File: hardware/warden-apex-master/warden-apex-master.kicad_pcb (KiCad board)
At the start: 4 copper layers, 100 x 100 mm, 72 parts, among them IC1 SIM7080G, IC2 BQ24650RVAR, IC3 TPS63070RNMR, IC4 MAX98357AETE+T, J1 U.FL-R-SMT-1, J2 U.FL-R-SMT-1, J3 61300211121, Q1 DMG9926UDM, Q2 AO3401A, Q3 2N7002, U1 113991115, U2 Ai-Thinker-Ra-01, U3 M138 Modem, U4 MCP23017_SO, U5 SRV05-4-P-T7, U6 SC16IS740, X1 14.7456MHz

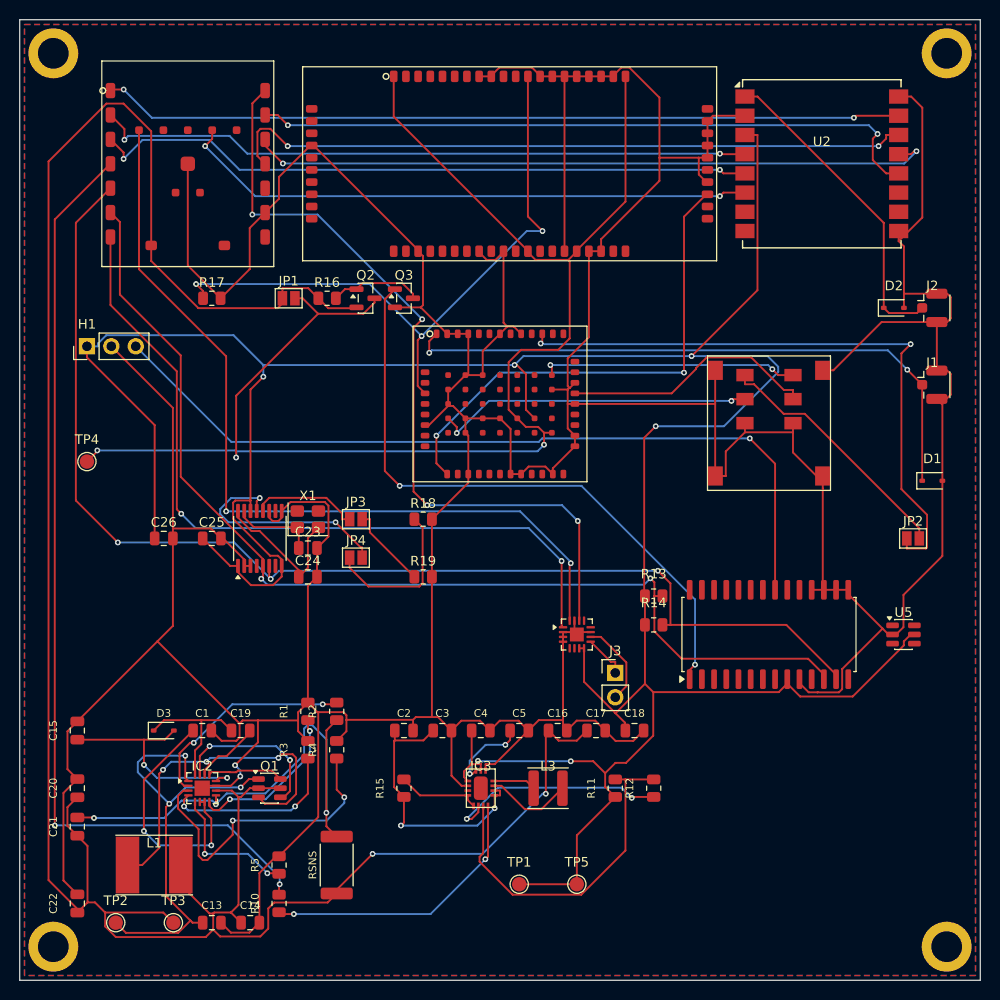
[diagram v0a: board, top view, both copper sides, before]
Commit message: Update warden-apex design with new components and net classifications. Added multiple capacitors (C27, C28, C29, C30, C31, C32) and a resistor (R23) to the schematic and PCB. Updated net classes for improved clarity and organization. Adjusted timestamps and documentation in PLAN.md and VARIANTS.md to reflect the latest changes.
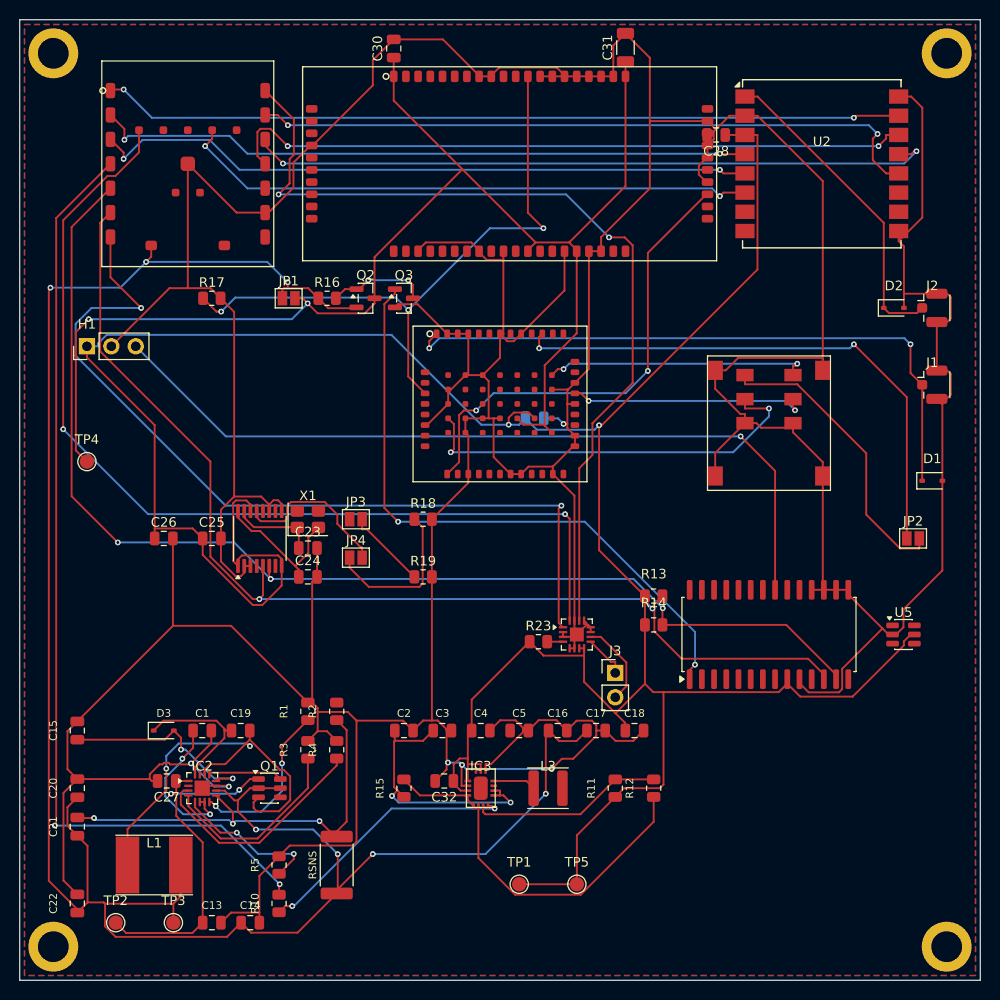
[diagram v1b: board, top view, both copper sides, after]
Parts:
- added C27: 100nF, Capacitor_SMD:C_0805_2012Metric, F.Cu at (15.3, 79.2)
- added C28: 100nF, Capacitor_SMD:C_0805_2012Metric, F.Cu at (72.5, 12.0)
- added C29: 100nF, Capacitor_SMD:C_0805_2012Metric, B.Cu at (53.6, 41.5)
- added C30: 100nF, Capacitor_SMD:C_0805_2012Metric, F.Cu at (38.9, 3.00)
- added C31: 47uF, C_1206_3216Metric, F.Cu at (63.1, 2.90)
- added C32: 10uF, Capacitor_SMD:C_0805_2012Metric, F.Cu at (44.2, 79.2)
- added R23: 100k, Resistor_SMD:R_0805_2012Metric, F.Cu at (54.0, 64.8)
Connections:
- IC4 pad 12: (no net) -> /GND
- IC4 pad 13: (no net) -> /GND
- IC4 pad 4: /GND -> /SD_MODE
- IC4 pad 5: (no net) -> /GND
- IC4 pad 6: (no net) -> /GND
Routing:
- net /GND: track 667.2 -> 736.5 mm, vias 2 -> 6
- net /VBAT_SYS: track 255.8 -> 226.4 mm, vias 2 -> 7
- net /MPPSET: track 22.6 -> 0.00 mm, vias 2 -> 0
- net /CHG_GATE_HI: track 16.8 -> 0.00 mm, vias 2 -> 0
- net /FB_DIV: track 35.9 -> 20.0 mm
- net /I2S_BCLK: track 87.7 -> 102.1 mm
- net /MODEM_VBAT_SW: track 155.0 -> 142.8 mm, vias 3 -> 2
- net /3V3: track 313.4 -> 302.0 mm, vias 6 -> 2
- net /U6_UART_TX: track 11.3 -> 0.00 mm
- net /I2S_LRCLK: track 82.8 -> 93.1 mm, vias 4 -> 2
- net /SOLAR_IN: track 47.5 -> 37.4 mm, vias 3 -> 2
- net /CHG_REF: track 25.5 -> 15.5 mm
- net /CHG_SENSE_NEG: track 54.0 -> 44.5 mm
- net /SIM_RST: track 33.4 -> 42.9 mm
- net /I2S_DOUT: track 80.5 -> 89.5 mm
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
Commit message: Update warden-apex design with new components including F1 (500mA PTC fuse), J4 (Expansion Header), and J5 (Qwiic connector). Adjusted resistor values and footprints for C31 and R24. Updated BOM files and Gerber generation timestamps to reflect the latest changes.
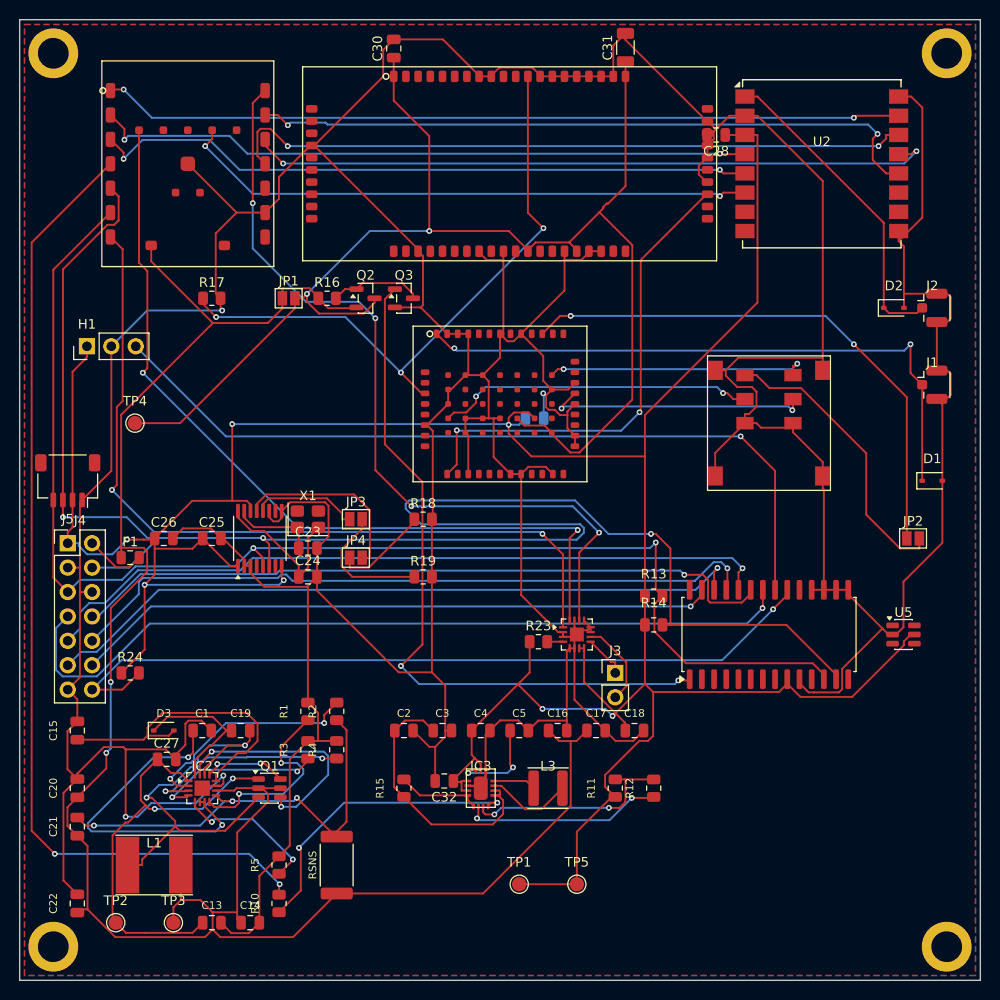
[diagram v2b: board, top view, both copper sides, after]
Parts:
- added F1: 500mA_PTC, Fuse_0805_2012Metric, F.Cu at (11.5, 56.0)
- added J4: Expansion_Header, PinHeader_2x07_P2.54mm_Vertical, F.Cu at (5.00, 54.5)
- added J5: Qwiic, JST_SH_SM04B-SRSS-TB_1x04-1MP_P1.00mm_Horizontal, F.Cu at (5.00, 48.0)
- added R24: 10k, R_0805_2012Metric, F.Cu at (11.5, 68.0)
- moved TP4 6.40 mm to (12.0, 42.0)
- moved C27 2.25 mm to (15.3, 77.0), turned to 0 degrees
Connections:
- IC2 pad : (no net) -> /GND
- IC3 pad 16: (no net) -> /GND
- IC4 pad : (no net) -> /GND
- U4 pad 20: (no net) -> /EXP_IRQ
- U4 pad 22: (no net) -> /EXP_GP1
- U4 pad 23: (no net) -> /EXP_GP2
- U4 pad 24: (no net) -> /EXP_GP3
- U4 pad 25: (no net) -> /EXP_GP4
- U4 pad 26: (no net) -> /EXP_GP5
- U4 pad 27: (no net) -> /EXP_GP6
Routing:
- net /EXP_GP1: track 0.00 -> 84.8 mm, vias 0 -> 1
- net /EXP_IRQ: track 0.00 -> 82.6 mm, vias 0 -> 1
- net /EXP_GP3: track 0.00 -> 77.7 mm, vias 0 -> 1
- net /EXP_GP5: track 0.00 -> 74.3 mm, vias 0 -> 1
- net /EXP_GP2: track 0.00 -> 74.0 mm, vias 0 -> 1
- net /EXP_GP4: track 0.00 -> 73.4 mm, vias 0 -> 1
- net /EXP_GP6: track 0.00 -> 67.1 mm, vias 0 -> 1
- net /I2C_SDA: track 124.0 -> 183.1 mm
- net /CHG_GATE_HI: track 0.00 -> 24.4 mm, vias 0 -> 2
- net /MPPSET: track 0.00 -> 23.6 mm, vias 0 -> 2
- net /3V3: track 302.0 -> 323.5 mm, vias 2 -> 7
- net /I2C_SCL: track 117.1 -> 138.1 mm
- net /CHG_REF: track 15.5 -> 34.8 mm
- net /VBAT_SYS: track 226.4 -> 210.1 mm, vias 7 -> 2
- net /I2S_BCLK: track 102.1 -> 87.7 mm
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
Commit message: Update warden-apex design with new resistor values and components. Changed C5 to 1uF and added resistors R20 (7.15k) and R21 (10k) to the schematic. Updated BOM files to reflect these changes and adjusted Gerber generation timestamps for consistency.
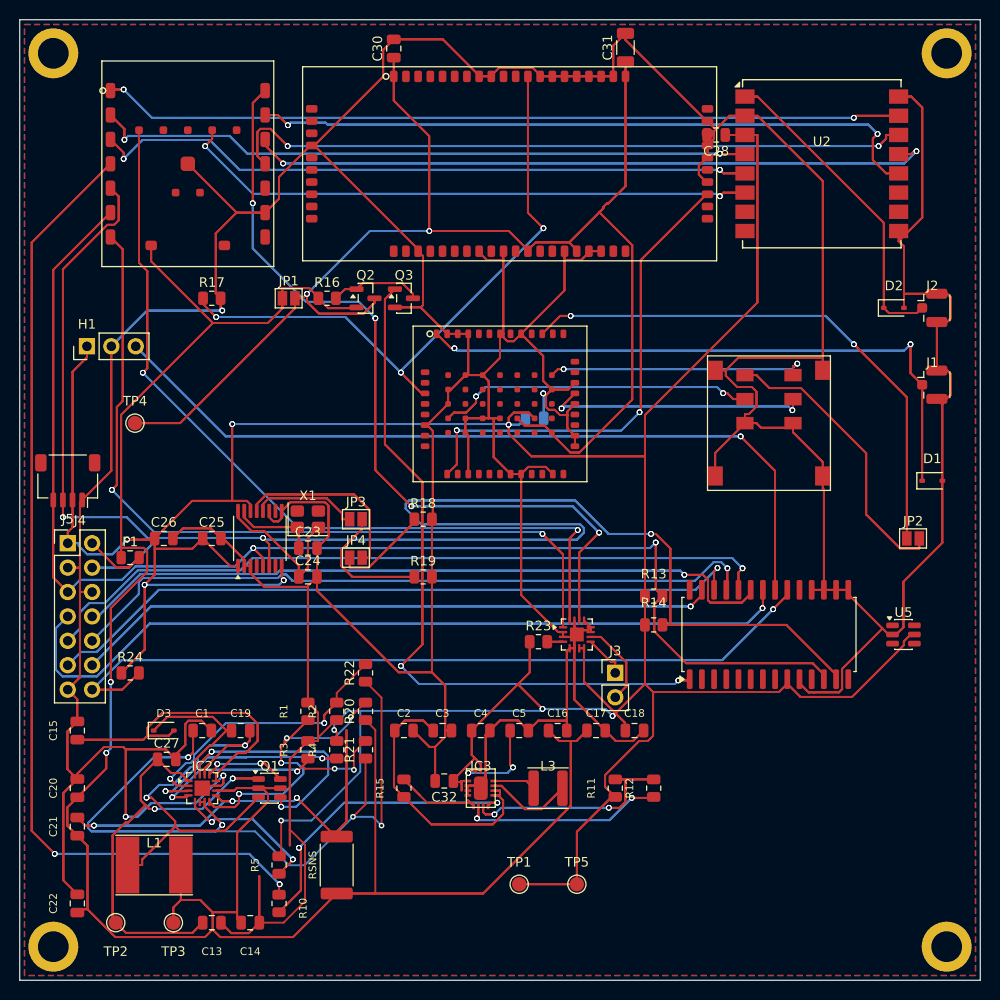
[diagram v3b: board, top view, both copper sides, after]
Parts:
- added R20: 7.15k, Resistor_SMD:R_0805_2012Metric, F.Cu at (36.0, 72.0)
- added R21: 10k, Resistor_SMD:R_0805_2012Metric, F.Cu at (36.0, 76.0)
- added R22: 100k, Resistor_SMD:R_0805_2012Metric, F.Cu at (36.0, 68.0)
- C5: value 100nF -> 1uF
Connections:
- IC3 pad 3: /3V3 -> /GND
- IC3 pad 4: /REG_EN -> /GND
- R2 pad 1: /CHG_SENSE_NEG -> /GND
- R4 pad 2: /GND -> /3V3
- R5 pad 2: /GND -> /3V3
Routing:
- net /GND: track 733.0 -> 1471.8 mm, vias 4 -> 8
- net /3V3: track 323.5 -> 690.3 mm, vias 7 -> 16
- net /VBAT_SYS: track 210.1 -> 438.7 mm, vias 2 -> 4
- net /I2C_SDA: track 183.1 -> 366.1 mm, vias 3 -> 6
- net /MODEM_VBAT_SW: track 143.5 -> 287.1 mm, vias 2 -> 4
- net /I2C_SCL: track 138.1 -> 276.2 mm, vias 2 -> 4
- net /PG_MON: track 102.1 -> 204.1 mm, vias 2 -> 4
- net /I2S_BCLK: track 87.7 -> 175.3 mm, vias 2 -> 4
- net /EXP_GP1: track 84.8 -> 169.5 mm, vias 1 -> 2
- net /I2S_DOUT: track 84.6 -> 169.3 mm, vias 2 -> 4
- net /I2S_LRCLK: track 84.6 -> 169.1 mm, vias 4 -> 8
- net /PIR_SIG: track 84.3 -> 168.6 mm, vias 1 -> 2
- net /LORA_NSS: track 83.4 -> 166.8 mm, vias 2 -> 4
- net /EXP_IRQ: track 82.6 -> 165.2 mm, vias 1 -> 2
- net /CHG_REF: track 34.8 -> 113.0 mm, vias 2 -> 6
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
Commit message: Update warden-apex design with revised net names and routing adjustments. Renamed net SIM_VDD_HOLDER to SIM_VDD_EXT and updated associated nodes. Adjusted timestamps in Gerber files and documentation for consistency. Added notes for manual routing requirements in README.md.
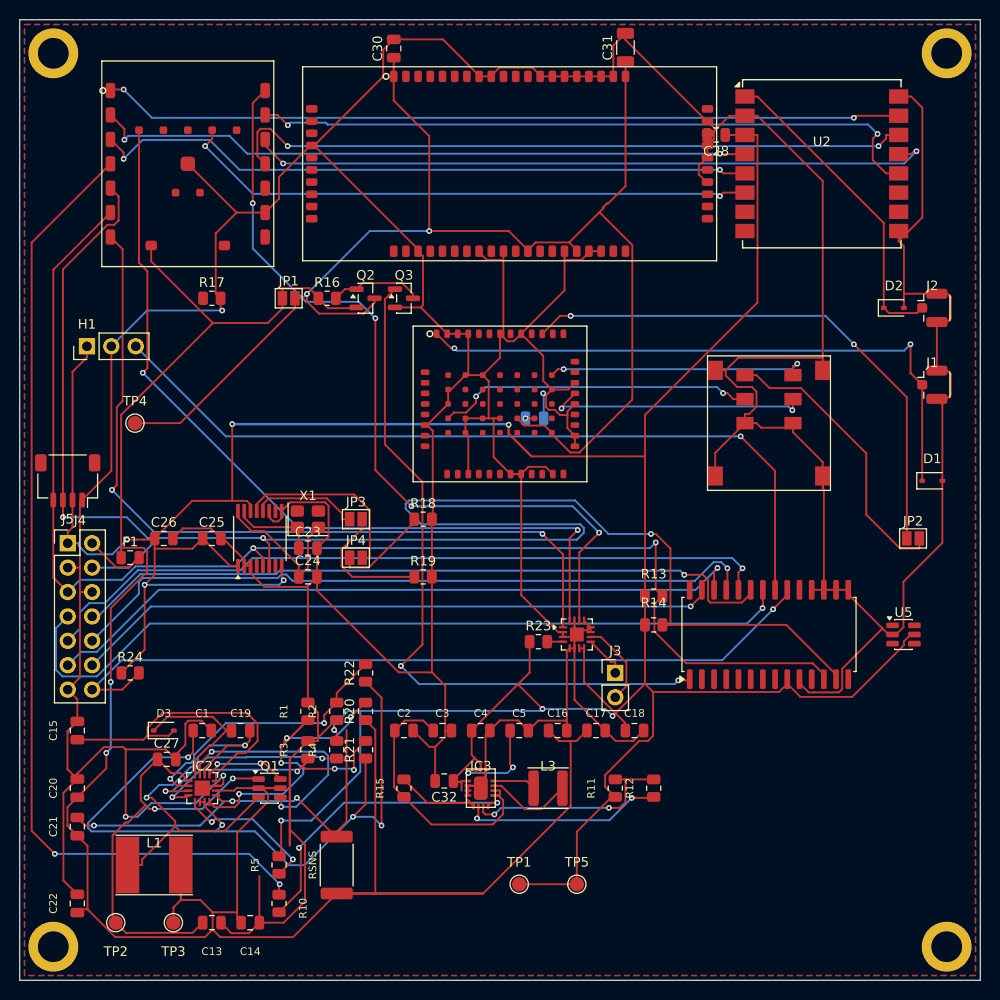
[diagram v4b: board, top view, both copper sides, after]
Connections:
- C29 pad 1: /3V3 -> /SIM_VDD_EXT
- IC1 pad 69: /3V3 -> /SIM_VDD_EXT
- IC2 pad : /GND -> (no net)
- IC4 pad : /GND -> (no net)
- U1 pad 18: (no net) -> /UART1_RX
- U1 pad 19: (no net) -> /UART1_TX
- U3 pad 12: /UART1_RX -> /UART2_RX
- U3 pad 28: /UART1_TX -> /UART2_TX
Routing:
- net /GND: track 1471.8 -> 758.6 mm, vias 8 -> 4
- net /3V3: track 690.3 -> 361.5 mm, vias 16 -> 9
- net /VBAT_SYS: track 438.7 -> 249.4 mm, vias 4 -> 2
- net /I2C_SDA: track 366.1 -> 183.1 mm, vias 6 -> 3
- net /MODEM_VBAT_SW: track 287.1 -> 143.5 mm, vias 4 -> 2
- net /I2C_SCL: track 276.2 -> 138.1 mm, vias 4 -> 2
- net /UART1_RX: track 130.3 -> 0.00 mm, vias 6 -> 0
- net /PG_MON: track 204.1 -> 102.1 mm, vias 4 -> 2
- net /UART1_TX: track 101.0 -> 0.00 mm, vias 4 -> 0
- net /I2S_BCLK: track 175.3 -> 87.7 mm, vias 4 -> 2
- net /EXP_GP1: track 169.5 -> 84.8 mm, vias 2 -> 1
- net /I2S_DOUT: track 169.3 -> 84.6 mm, vias 4 -> 2
- net /I2S_LRCLK: track 169.1 -> 84.6 mm, vias 8 -> 4
- net /PIR_SIG: track 168.6 -> 84.3 mm, vias 2 -> 1
- net /LORA_NSS: track 166.8 -> 83.4 mm, vias 4 -> 2
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- added copper zone on B.Cu, net /GND
- added copper zone on F.Cu, net /GND
- added copper zone on In1.Cu, net /GND
- added copper zone on In2.Cu, net /VBAT_SYS
- removed copper zone on B.Cu, net GND
- removed copper zone on F.Cu, net GND
- removed copper zone on In1.Cu, net GND
- removed copper zone on In2.Cu, net VBAT_SYS

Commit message: Update warden-apex design for Phase 21 SIM7080 repair. Adjusted BOM files to include new capacitor C33 and updated component placements for C34. Revised Gerber files with new timestamps and corrected net connections for UART signals. Enhanced README.md with details on the repair process and updated upload instructions for JLCPCB.
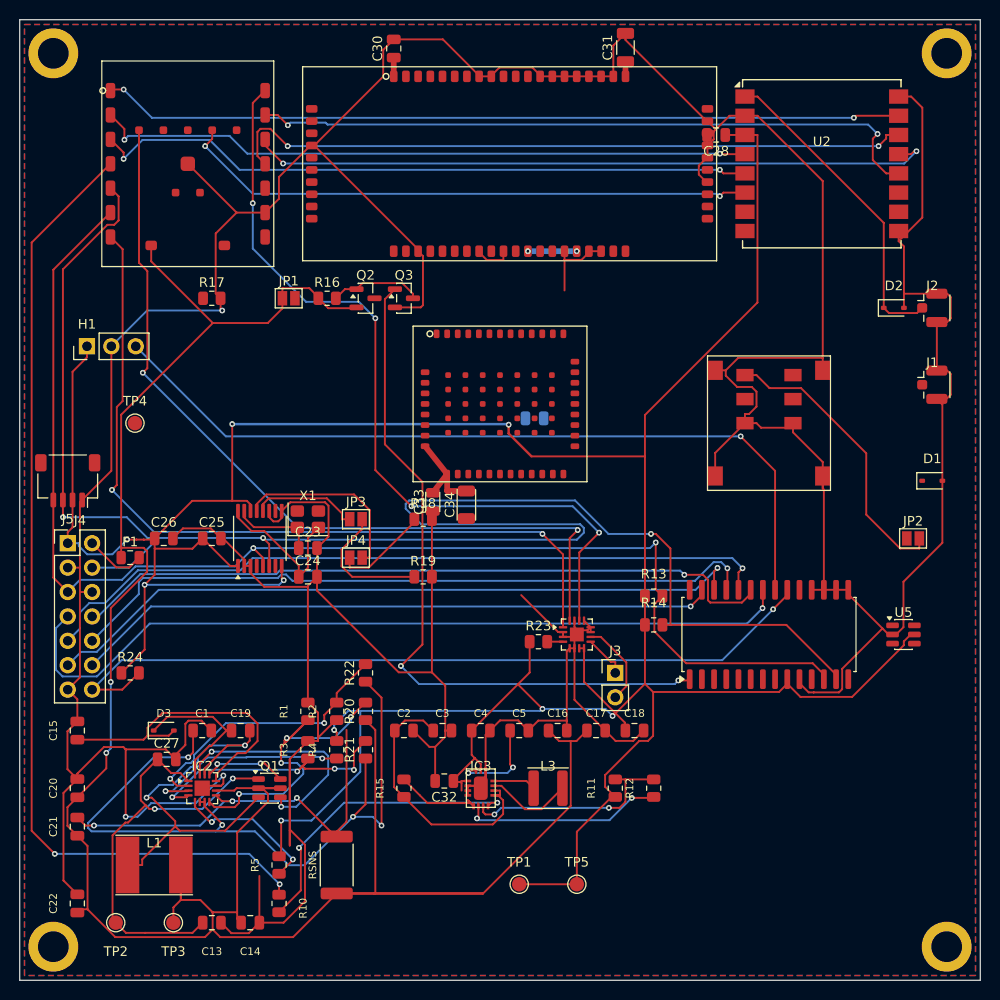
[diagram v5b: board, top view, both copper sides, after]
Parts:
- added C33: 100nF, Capacitor_SMD:C_0805_2012Metric, F.Cu at (43.0, 50.2)
- added C34: 47uF, Capacitor_SMD:C_1206_3216Metric, F.Cu at (46.5, 50.5)
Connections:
- IC1 pad 1: /CELL_RF -> /UART1_RX
- IC1 pad 10: (no net) -> /GND
- IC1 pad 11: /SIM_VDD -> /GND
- IC1 pad 12: (no net) -> /GND
- IC1 pad 13: (no net) -> /GND
- IC1 pad 14: (no net) -> /GND
- IC1 pad 15: (no net) -> /SIM_DATA
- IC1 pad 16: /GND -> /SIM_CLK
- IC1 pad 17: /SIM_DATA -> /SIM_RST
- IC1 pad 18: /GND -> /SIM_VDD
- IC1 pad 19: (no net) -> /GND
- IC1 pad 2: /GND -> /UART1_TX
- IC1 pad 20: (no net) -> /GND
- IC1 pad 23: (no net) -> /GND
- IC1 pad 25: (no net) -> /GND
- IC1 pad 26: (no net) -> /GND
- IC1 pad 29: (no net) -> /GND
- IC1 pad 30: (no net) -> /GND
- IC1 pad 31: (no net) -> /GND
- IC1 pad 32: /GND -> /CELL_RF
- IC1 pad 33: (no net) -> /GND
- IC1 pad 34: /UART1_TX -> /MODEM_VBAT_SW
- IC1 pad 35: (no net) -> /MODEM_VBAT_SW
- IC1 pad 36: (no net) -> /GND
- IC1 pad 38: (no net) -> /GND
- IC1 pad 39: (no net) -> /GND
- IC1 pad 40: /UART1_RX -> /SIM_VDD_EXT
- IC1 pad 41: (no net) -> /GND
- IC1 pad 42: (no net) -> /GND
- IC1 pad 43: (no net) -> /GND
- IC1 pad 46: (no net) -> /GND
- IC1 pad 47: (no net) -> /GND
- IC1 pad 48: (no net) -> /GND
- IC1 pad 49: /SIM_CLK -> /GND
- IC1 pad 5: (no net) -> /GND
- IC1 pad 51: (no net) -> /GND
- IC1 pad 52: (no net) -> /GND
- IC1 pad 53: (no net) -> /GND
- IC1 pad 54: (no net) -> /GND
- IC1 pad 55: (no net) -> /GND
- IC1 pad 58: (no net) -> /GND
- IC1 pad 59: (no net) -> /GND
- IC1 pad 6: (no net) -> /GND
- IC1 pad 60: (no net) -> /GND
- IC1 pad 61: (no net) -> /GND
- IC1 pad 62: (no net) -> /GND
- IC1 pad 63: (no net) -> /GND
- IC1 pad 64: /SIM_RST -> /GND
- IC1 pad 68: /MODEM_VBAT_SW -> /GND
- IC1 pad 69: /SIM_VDD_EXT -> /GND
- IC1 pad 70: (no net) -> /GND
- IC1 pad 71: (no net) -> /GND
- IC1 pad 73: (no net) -> /GND
- IC1 pad 74: (no net) -> /GND
- IC1 pad 75: (no net) -> /GND
- IC1 pad 76: (no net) -> /GND
- IC1 pad 77: /MODEM_VBAT_SW -> /GND
- IC1 pad 8: (no net) -> /GND
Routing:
- net /MODEM_VBAT_SW: track 143.5 -> 18.5 mm
- net /GND: track 758.6 -> 646.2 mm, vias 4 -> 3
- net /CELL_RF: track 65.0 -> 0.00 mm, vias 2 -> 0
- net /SIM_VDD: track 56.9 -> 0.00 mm, vias 2 -> 0
- net /SIM_RST: track 33.1 -> 0.00 mm, vias 2 -> 0
- net /SIM_DATA: track 27.6 -> 0.00 mm, vias 2 -> 0
- net /SIM_CLK: track 27.5 -> 0.00 mm, vias 2 -> 0
- net /SIM_VDD_EXT: track 0.95 -> 0.00 mm, vias 1 -> 0
